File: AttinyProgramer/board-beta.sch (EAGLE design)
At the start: 11 parts, among them IC1 ATTINY44-SSU

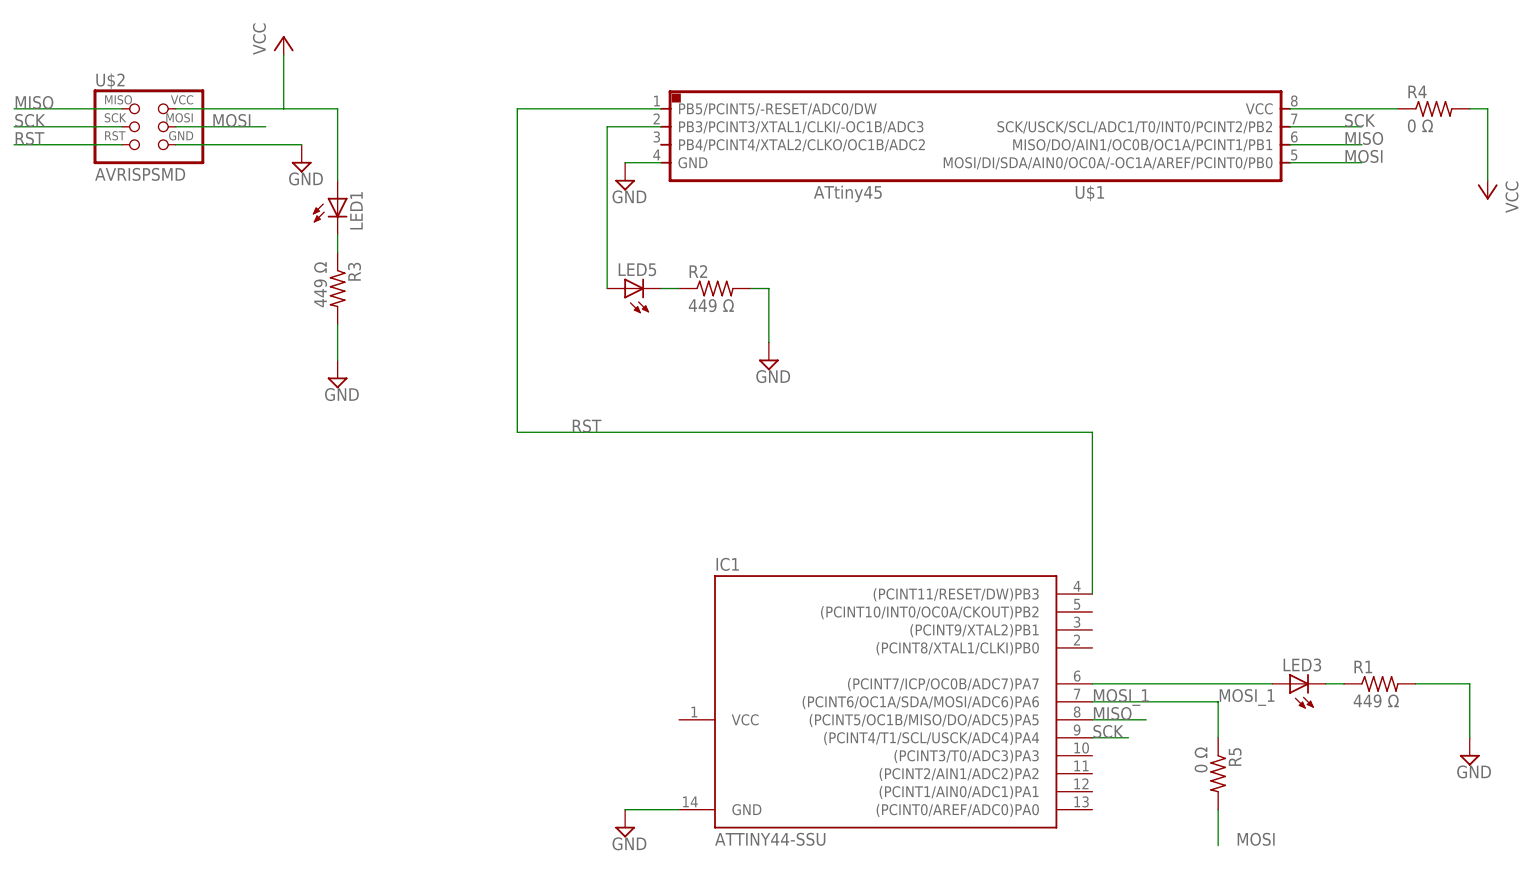
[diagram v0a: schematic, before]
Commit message: add board programer bootloader
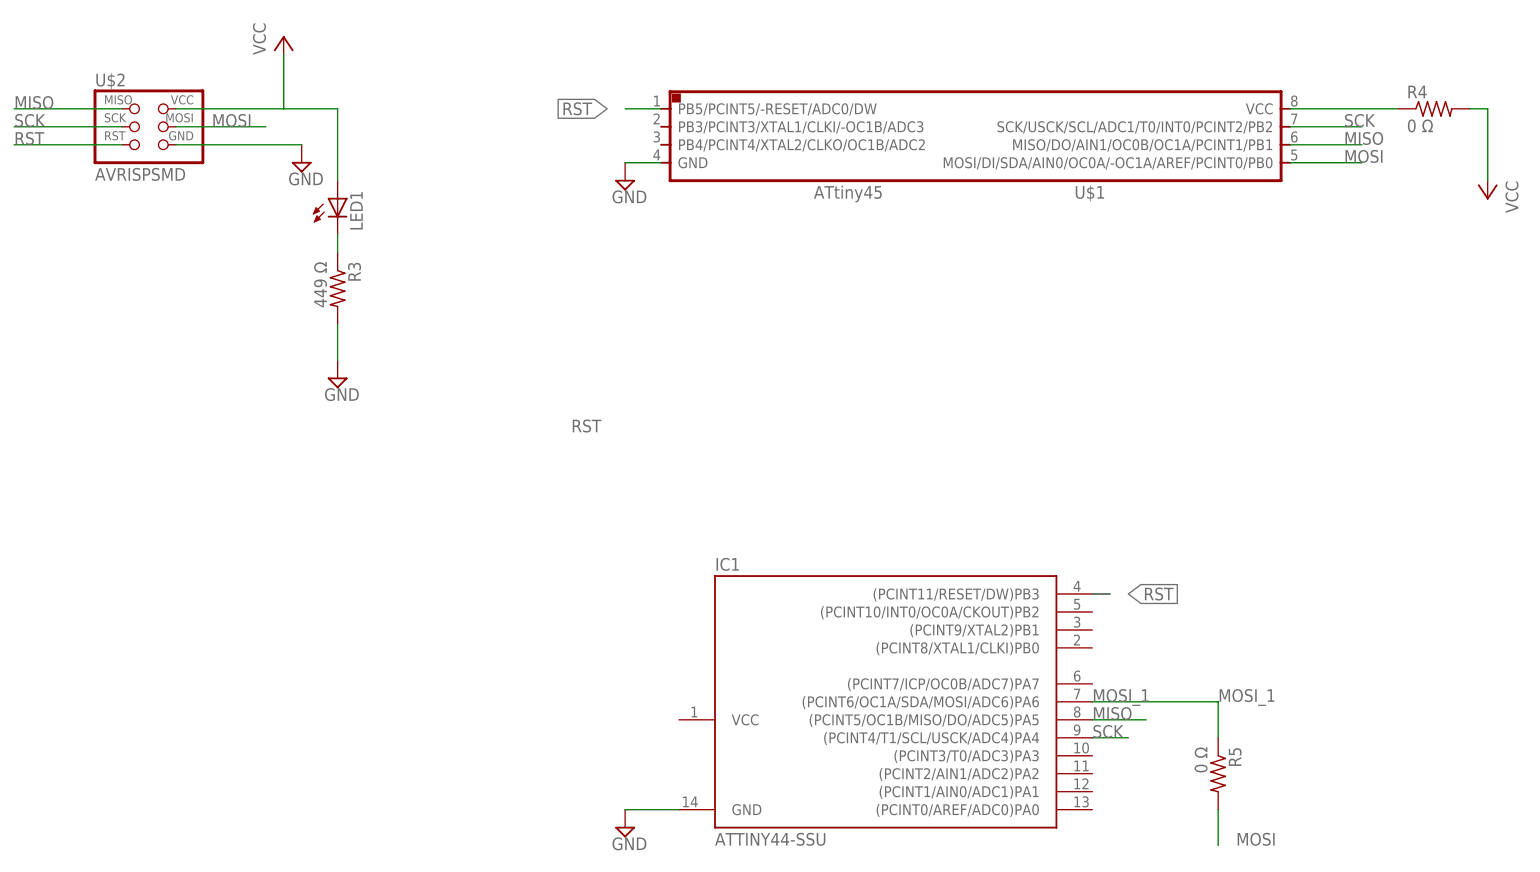
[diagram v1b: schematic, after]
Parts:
- removed LED3, LED5: (no value), adafruit:LEDCHIPLED_1206
- removed R1, R2: 449 Ω, fab:RES-US1206
- R3, R4, R5: device fab:RES-US1206 -> fab:RES-US1206FAB
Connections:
- removed net N$10: IC1.(PCINT7/ICP/OC0B/ADC7)PA7, LED3.A
- removed net N$4: LED3.C, R1.1
- removed net N$6: LED5.C, R2.1
- removed net N$7: LED5.A, U$1.PB3/PCINT3/XTAL1/CLKI/-OC1B/ADC3
- net GND: no longer R1.2, R2.2
